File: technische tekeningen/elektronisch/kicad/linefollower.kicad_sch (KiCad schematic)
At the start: 19 parts, among them J1 XT30, M1 N20 10:1 encoder (links), M2 N20 10:1 encoder (rechts), SW1 Power SS12D00, SW2 Start/Stop, U1 ESP32-S3-DevKitC-1 N8R2, U2 CN3903 3,3V, U3 Pololu QTR-8A, U4 TB6612FNG

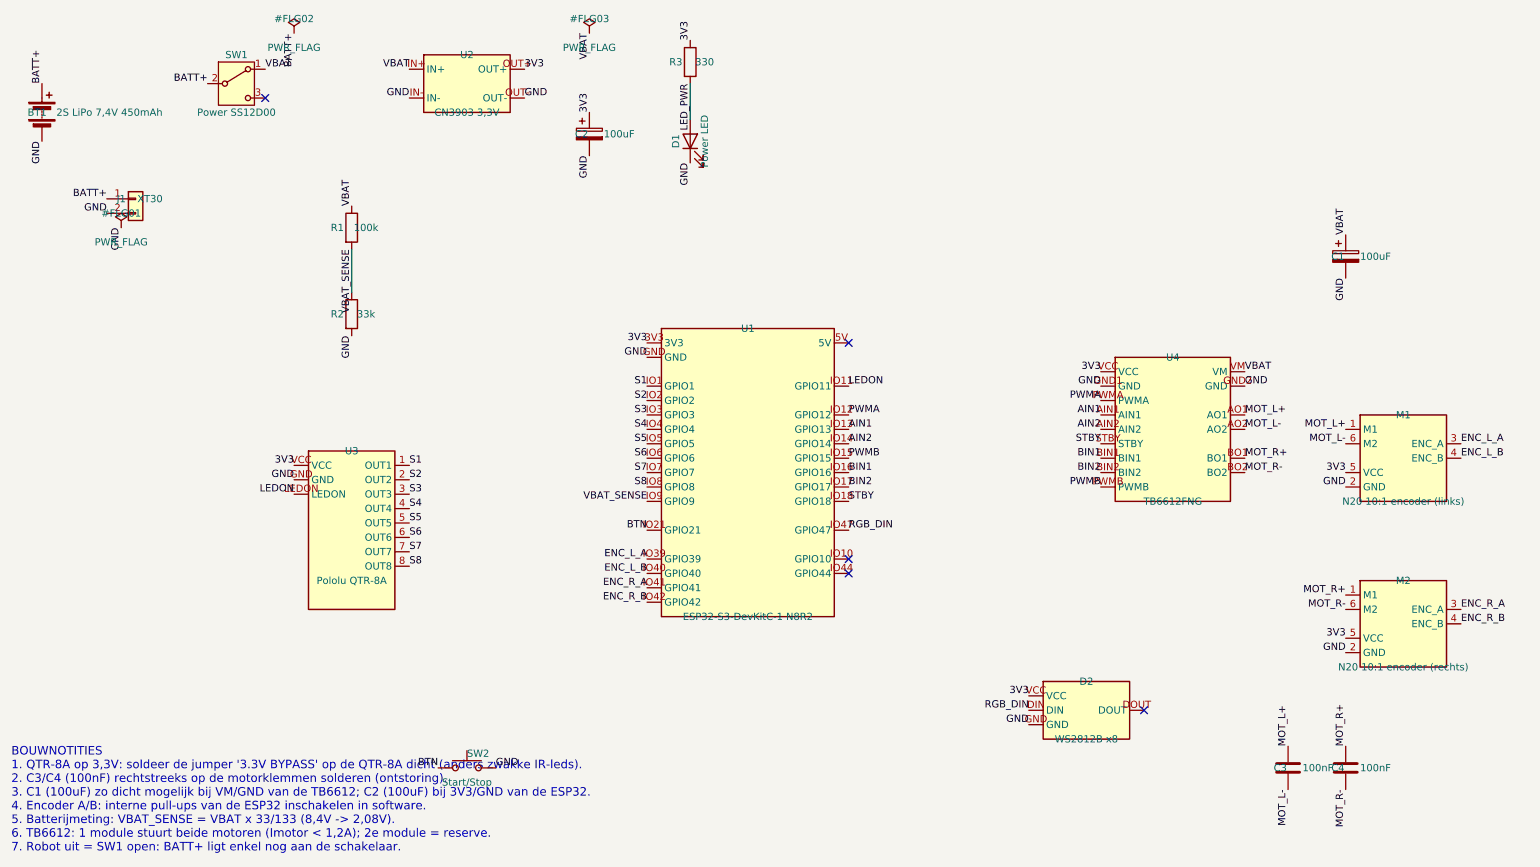
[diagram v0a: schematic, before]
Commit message: Tekeningen naar echte onderdelen, bekabelingsplan, bouwplan en readme per map
- Elektrisch schema rev 1.1: WS2812 weg (niet besteld), status via ingebouwde RGB-led (GPIO48), waarden = bestelde onderdelen, PDF + SVG
- 3D-model parametrisch (model_linefollower.py): Pololu-maten uit de maattekeningen, AliExpress-maten na te meten; print ingekort tot 120 mm, spoiler uit het afgezaagde stuk
- Boormal 1:1, bekabelingsplan 2:1 met 48 genummerde draden en draadlijst per bouwstap (bekabelingsplan.py)
- Instructable: 13 stappen met test per stap
- Readme in elke map, gebruiksaanwijzing, datasheets, PoC-uitleg
- Tekenscript 30x sneller, PDF 13 MB -> 0,2 MB

Co-Authored-By: Claude Opus 5.5 <noreply@anthropic.com>
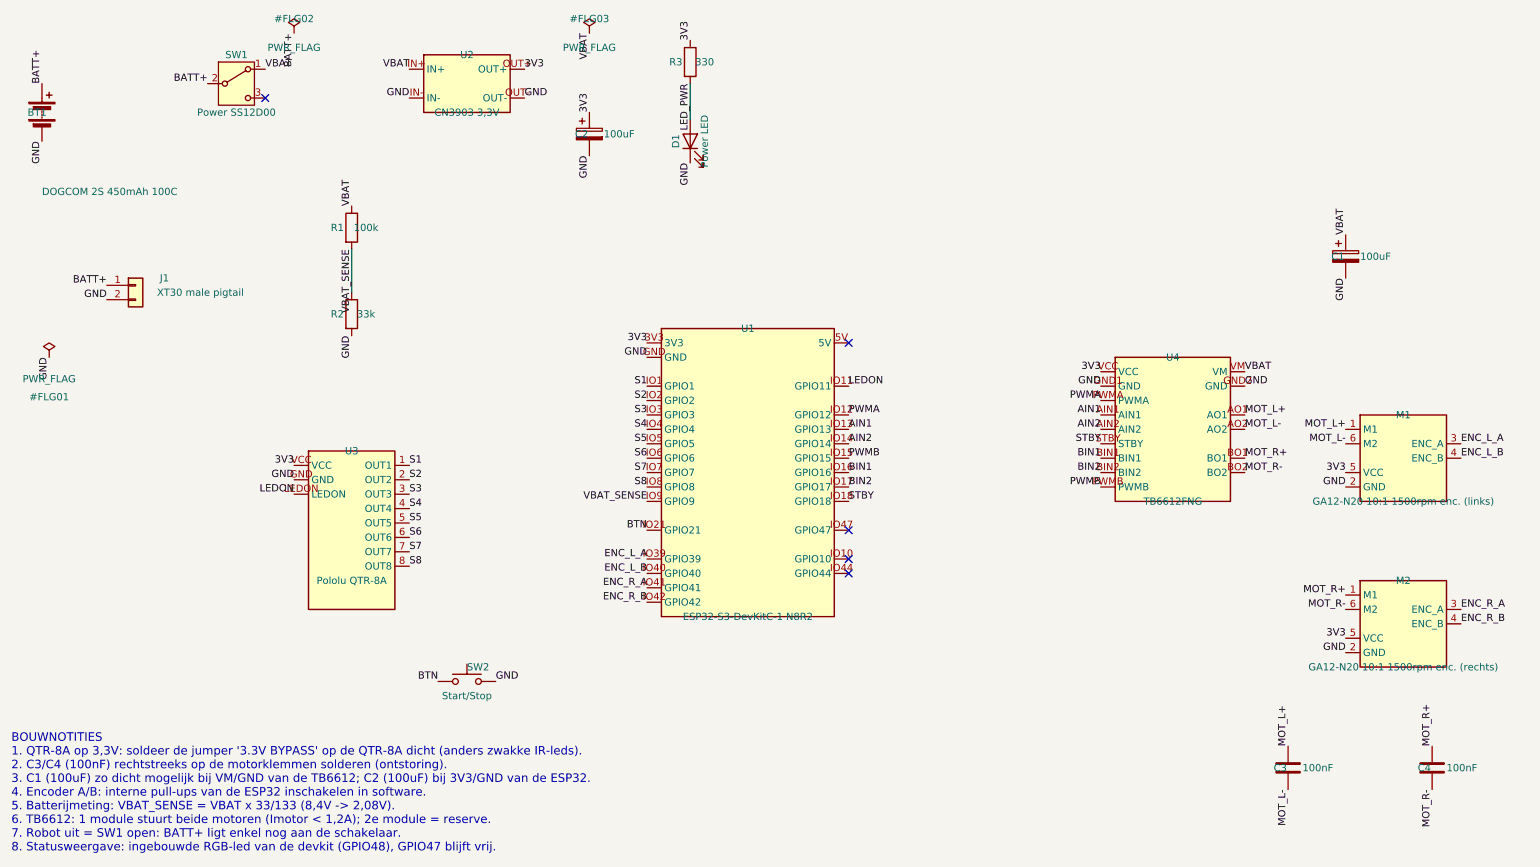
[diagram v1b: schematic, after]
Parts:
- removed D2: WS2812B x8, symbol lf_modules:WS2812_Stick_8
- BT1: value 2S LiPo 7,4V 450mAh -> DOGCOM 2S 450mAh 100C
- J1: value XT30 -> XT30 male pigtail
- M1: value N20 10:1 encoder (links) -> GA12-N20 10:1 1500rpm enc. (links)
- M2: value N20 10:1 encoder (rechts) -> GA12-N20 10:1 1500rpm enc. (rechts)
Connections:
- net RGB_DIN: no longer names the net of U1.IO47 (GPIO47)
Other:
- moved on the sheet: C4, J1, SW2
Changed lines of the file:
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@@
 	(title_block
 		(title "Linefollower - elektrisch schema (plan B, gaatjesprint)")
-		(date "2026-10-08")
-		(rev "1.0")
+		(date "2026-10-19")
+		(rev "1.1")
 		(company "HOGENT Elektromechanica - Albin")
 		(comment 1 "ESP32-S3 + QTR-8A + TB6612FNG + 2x N20 10:1 met encoder, 2S LiPo")
-		(comment 2 "Pinverdeling: zie ontwerpkeuzes/onderdelenkeuze.md")
+		(comment 2 "Onderdelen = bestelling 19/10/2026; status-led = RGB op devkit (GPIO48)")
 	)
 	(symbol
@@
 			)
 		)
-		(property "Value" "2S LiPo 7,4V 450mAh"
-			(at 27.94 44.45 0)
+		(property "Value" "DOGCOM 2S 450mAh 100C"
+			(at 25.4 58.42 0)
 			(show_name no)
 			(do_not_autoplace no)
@@
 	(symbol
 		(lib_id "Connector_Generic:Conn_01x02")
-		(at 41.91 59.69 0)
+		(at 41.91 74.93 0)
 		(unit 1)
 		(body_style 1)
@@
 		(dnp no)
 		(property "Reference" "J1"
-			(at 39.37 59.69 0)
-			(show_name no)
-			(do_not_autoplace no)
-			(effects
-				(font
-					(size 1.27 1.27)
-				)
-			)
-		)
-		(property "Value" "XT30"
-			(at 44.449999999999996 59.69 0)
+			(at 46.99 73.66 0)
+			(show_name no)
+			(do_not_autoplace no)
+			(effects
+				(font
+					(size 1.27 1.27)
+				)
+			)
+		)
+		(property "Value" "XT30 male pigtail"
+			(at 53.34 76.2 0)
 			(show_name no)
 			(do_not_autoplace no)
@@
 		)
 		(property "Footprint" ""
-			(at 41.91 59.69 0)
+			(at 41.91 74.93 0)
 			(hide yes)
 			(show_name no)
@@
 		)
 		(property "Datasheet" ""
-			(at 41.91 59.69 0)
+			(at 41.91 74.93 0)
 			(hide yes)
 			(show_name no)
@@
 		)
 		(property "Description" "Generic connector, single row, 01x02, script generated (kicad-library-utils/schlib/autogen/connector/)"
-			(at 41.91 59.69 0)
+			(at 41.91 74.93 0)
 			(hide yes)
 			(show_name no)
@@
 	(symbol
 		(lib_id "Switch:SW_Push")
-		(at 100.33 160.02 0)
+		(at 100.33 144.78 0)
 		(unit 1)
 		(body_style 1)
@@
 		(dnp no)
 		(property "Reference" "SW2"
-			(at 100.33 157.48 0)
+			(at 100.33 142.24 0)
 			(show_name no)
 			(do_not_autoplace no)
@@
 		)
 		(property "Value" "Start/Stop"
-			(at 100.33 162.56 0)
+			(at 100.33 147.32 0)
 			(show_name no)
 			(do_not_autoplace no)
@@
 		)
 		(property "Footprint" ""
-			(at 100.33 165.1 0)
+			(at 100.33 149.86 0)
 			(hide yes)
 			(show_name no)
@@
 		)
 		(property "Datasheet" ""
-			(at 100.33 165.1 0)
+			(at 100.33 149.86 0)
 			(hide yes)
 			(show_name no)
@@
 		)
 		(property "Description" "Push button switch, generic, two pins"
-			(at 100.33 160.02 0)
+			(at 100.33 144.78 0)
 			(hide yes)
 			(show_name no)
@@
 			)
 		)
-		(property "Value" "N20 10:1 encoder (links)"
+		(property "Value" "GA12-N20 10:1 1500rpm enc. (links)"
 			(at 265.43 113.03 0)
 			(show_name no)
@@
 			)
 		)
-		(property "Value" "N20 10:1 encoder (rechts)"
+		(property "Value" "GA12-N20 10:1 1500rpm enc. (rechts)"
 			(at 265.43 142.24 0)
 			(show_name no)
@@
 	(symbol
 		(lib_id "Device:C")
-		(at 255.27 160.02 0)
+		(at 270.51 160.02 0)
 		(unit 1)
 		(body_style 1)
@@
 		(dnp no)
 		(property "Reference" "C4"
-			(at 252.73 160.02 0)
+			(at 267.97 160.02 0)
 			(show_name no)
 			(do_not_autoplace no)
@@
 		)
 		(property "Value" "100nF"
-			(at 257.81 160.02 0)
+			(at 273.05 160.02 0)
 			(show_name no)
 			(do_not_autoplace no)
@@
 		)
 		(property "Footprint" ""
-			(at 256.235 156.21 0)
+			(at 271.48 156.21 0)
 			(hide yes)
 			(show_name no)
@@
 		)
 		(property "Datasheet" ""
-			(at 255.27 160.02 0)
+			(at 270.51 160.02 0)
 			(hide yes)
 			(show_name no)
@@
 		)
 		(property "Description" "Unpolarized capacitor"
-			(at 255.27 160.02 0)
+			(at 270.51 160.02 0)
 			(hide yes)
 			(show_name no)
@@
 	)
 	(symbol
-		(lib_id "lf_modules:WS2812_Stick_8")
-		(at 209.55 149.86 0)
-		(unit 1)
-		(body_style 1)
-		(exclude_from_sim no)
-		(in_bom yes)
-		(on_board yes)
-		(in_pos_files yes)
-		(dnp no)
-		(property "Reference" "D2"
-			(at 209.55 144.78 0)
-			(show_name no)
-			(do_not_autoplace no)
-			(effects
-				(font
-					(size 1.27 1.27)
-				)
-			)
-		)
-		(property "Value" "WS2812B x8"
-			(at 209.55 154.94 0)
-			(show_name no)
-			(do_not_autoplace no)
-			(effects
-				(font
-					(size 1.27 1.27)
-				)
-			)
-		)
-		(property "Footprint" ""
-			(at 209.55 144.78 0)
-			(hide yes)
-			(show_name no)
-			(do_not_autoplace no)
-			(effects
-				(font
-					(size 1.27 1.27)
-				)
-			)
-		)
-		(property "Datasheet" ""
-			(at 209.55 142.24 0)
-			(hide yes)
-			(show_name no)
-			(do_not_autoplace no)
-			(effects
-				(font
-					(size 1.27 1.27)
-				)
-			)
-		)
-		(property "Description" "WS2812B strip 8 leds (sensorweergave/status)"
-			(at 209.55 139.7 0)
-			(hide yes)
-			(show_name no)
-			(do_not_autoplace no)
-			(effects
-				(font
-					(size 1.27 1.27)
-				)
-			)
-		)
-		(pin "DIN"
-		)
-		(pin "DOUT"
-		)
-		(pin "GND"
-		)
-		(pin "VCC"
-		)
-		(instances
-			(project "linefollower"
-				(path "/82139a58-5523-4d04-8a5f-a6de3939ef82"
-					(reference "D2")
-					(unit 1)
-				)
-			)
-		)
-	)
-	(symbol
 		(lib_id "power:PWR_FLAG")
-		(at 39.37 64.77 0)
+		(at 26.67 87.63 0)
 		(unit 1)
 		(body_style 1)
@@
 		(dnp no)
 		(property "Reference" "#FLG01"
-			(at 39.37 62.23 0)
+			(at 26.67 94.62 0)
 			(show_name no)
 			(do_not_autoplace no)
@@
 		)
 		(property "Value" "PWR_FLAG"
-			(at 39.37 67.31 0)
+			(at 26.67 91.44 0)
 			(show_name no)
 			(do_not_autoplace no)
@@
 		)
 		(property "Footprint" ""
-			(at 39.37 64.77 0)
+			(at 26.67 91.44 0)
 			(hide yes)
 			(show_name no)
@@
 		)
 		(property "Datasheet" ""
-			(at 39.37 64.77 0)
+			(at 26.67 91.44 0)
 			(hide yes)
 			(show_name no)
@@
 		)
 		(property "Description" "Special symbol for telling ERC where power comes from"
-			(at 39.37 64.77 0)
+			(at 26.67 91.44 0)
 			(hide yes)
 			(show_name no)
@@
 	)
 	(label "BATT+"
-		(at 36.83 59.69 180)
+		(at 36.83 74.93 180)
 		(effects
 			(font
@@
 	)
 	(label "GND"
-		(at 36.83 62.23 180)
+		(at 36.83 77.47 180)
 		(effects
 			(font
@@
 		)
 	)
-	(label "RGB_DIN"
-		(at 167.64000000000001 118.11 0)
-		(effects
-			(font
-				(size 1.27 1.27)
-			)
-			(justify left bottom)
-		)
-	)
 	(label "S1"
 		(at 90.17 106.67999999999999 0)
@@
 	)
 	(label "BTN"
-		(at 95.25 160.02 180)
+		(at 95.25 144.78 180)
 		(effects
 			(font
@@
 	)
 	(label "GND"
-		(at 105.41 160.02 0)
+		(at 105.41 144.78 0)
 		(effects
 			(font
@@
 	)
 	(label "MOT_R+"
-		(at 255.27 156.21 90)
+		(at 270.51 156.21 90)
 		(effects
 			(font
@@
 	)
 	(label "MOT_R-"
-		(at 255.27 163.83 270)
-		(effects
-			(font
-				(size 1.27 1.27)
-			)
-			(justify right bottom)
-		)
-	)
-	(label "3V3"
-		(at 199.39000000000001 147.32000000000002 180)
+		(at 270.51 163.83 270)
 		(effects
 			(font
@@
 	)
 	(label "GND"
-		(at 199.39000000000001 152.4 180)
-		(effects
-			(font
-				(size 1.27 1.27)
-			)
-			(justify right bottom)
-		)
-	)
-	(label "RGB_DIN"
-		(at 199.39000000000001 149.86 180)
-		(effects
-			(font
-				(size 1.27 1.27)
-			)
-			(justify right bottom)
-		)
-	)
-	(label "GND"
-		(at 39.37 64.77 270)
+		(at 26.67 87.63 270)
 		(effects
 			(font
@@
 	)
 	(no_connect
+		(at 167.64 118.11)
+	)
+	(no_connect
 		(at 64.77 41.91)
 	)
@@
 		(at 167.64000000000001 125.72999999999999)
 	)
-	(no_connect
-		(at 219.71 149.86)
-	)
-	(text "BOUWNOTITIES\n1. QTR-8A op 3,3V: soldeer de jumper '3.3V BYPASS' op de QTR-8A dicht (anders zwakke IR-leds).\n2. C3/C4 (100nF) rechtstreeks op de motorklemmen solderen (ontstoring).\n3. C1 (100uF) zo dicht mogelijk bij VM/GND van de TB6612; C2 (100uF) bij 3V3/GND van de ESP32.\n4. Encoder A/B: interne pull-ups van de ESP32 inschakelen in software.\n5. Batterijmeting: VBAT_SENSE = VBAT x 33/133 (8,4V -> 2,08V).\n6. TB6612: 1 module stuurt beide motoren (Imotor < 1,2A); 2e module = reserve.\n7. Robot uit = SW1 open: BATT+ ligt enkel nog aan de schakelaar."
+	(text "BOUWNOTITIES\n1. QTR-8A op 3,3V: soldeer de jumper '3.3V BYPASS' op de QTR-8A dicht (anders zwakke IR-leds).\n2. C3/C4 (100nF) rechtstreeks op de motorklemmen solderen (ontstoring).\n3. C1 (100uF) zo dicht mogelijk bij VM/GND van de TB6612; C2 (100uF) bij 3V3/GND van de ESP32.\n4. Encoder A/B: interne pull-ups van de ESP32 inschakelen in software.\n5. Batterijmeting: VBAT_SENSE = VBAT x 33/133 (8,4V -> 2,08V).\n6. TB6612: 1 module stuurt beide motoren (Imotor < 1,2A); 2e module = reserve.\n7. Robot uit = SW1 open: BATT+ ligt enkel nog aan de schakelaar.\n8. Statusweergave: ingebouwde RGB-led van de devkit (GPIO48), GPIO47 blijft vrij."
 		(exclude_from_sim no)
 		(at 20 175 0)
